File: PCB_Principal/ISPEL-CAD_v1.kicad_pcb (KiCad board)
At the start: 2 copper layers, 130 x 160 mm, 175 parts, among them J1 Vin, J10 CN7_NUCLEO, J11 CN10_NUCLEO, J12 GND_NUCLEO, J13 E1, J14 S1, J15 E2, J16 S2, J17 FRENTE, J18 PRUEBA_5V, J2 V5, J3 VREG, J4 TEMP, J5 GND_NUCLEO, J6 CN8_NUCLEO, J7 CN9_NUCLEO, J8 GND_NUCLEO, J9 GND_NUCLEO, Q201 BC807, Q202 BC559C, Q203 BC549C, Q204 BC549C, Q205 BC559C, Q206 2SD882, Q207 2SB772, Q251 BC807, Q252 BC559C, Q253 BC549C, Q254 BC549C, Q255 BC559C, Q256 2SD882, Q257 2SB772, U1 LM350_TO220, U101 TL071, U151 TL071, U2 LM350_TO220, U201 LM318, U251 LM318, U3 LM337_TO220, U301 TLV3501AID, U4 LM1117DT-5.0, U5 TL431DBZ

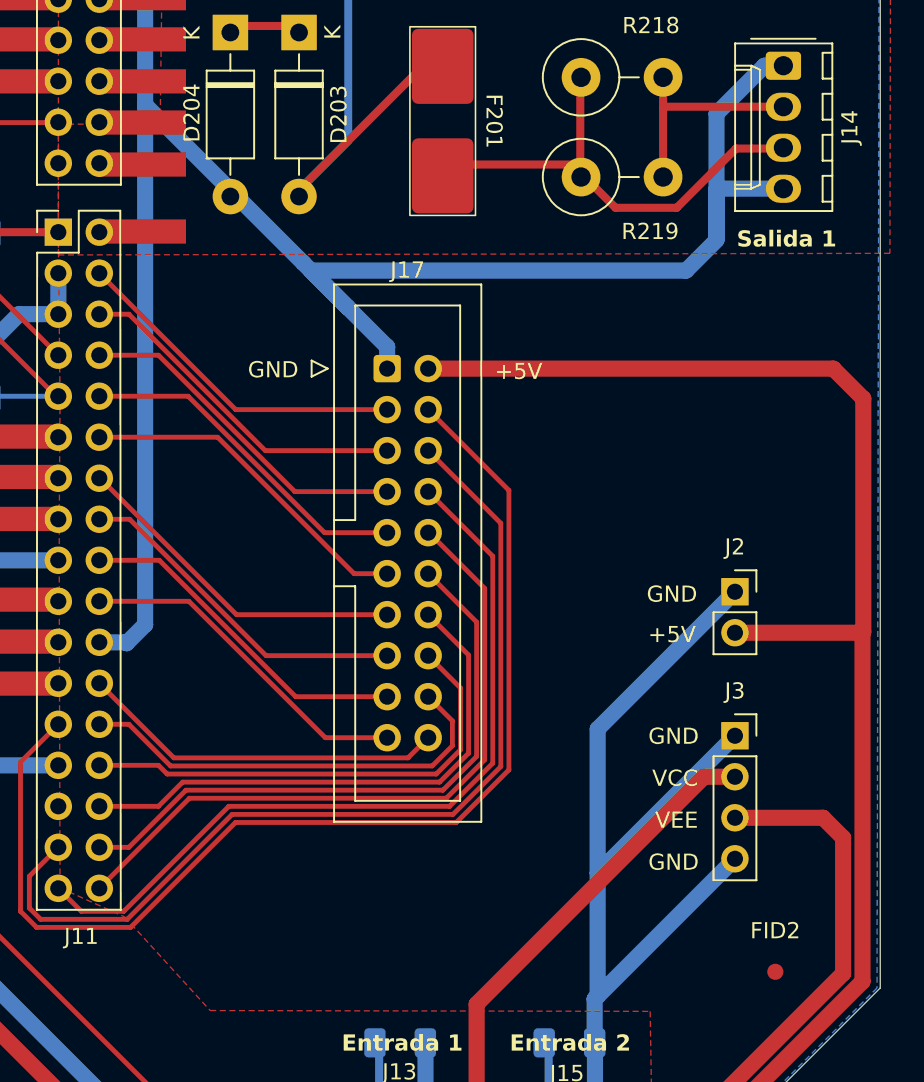
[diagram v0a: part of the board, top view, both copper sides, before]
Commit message: Corrigiendo PCB con comentarios AS.
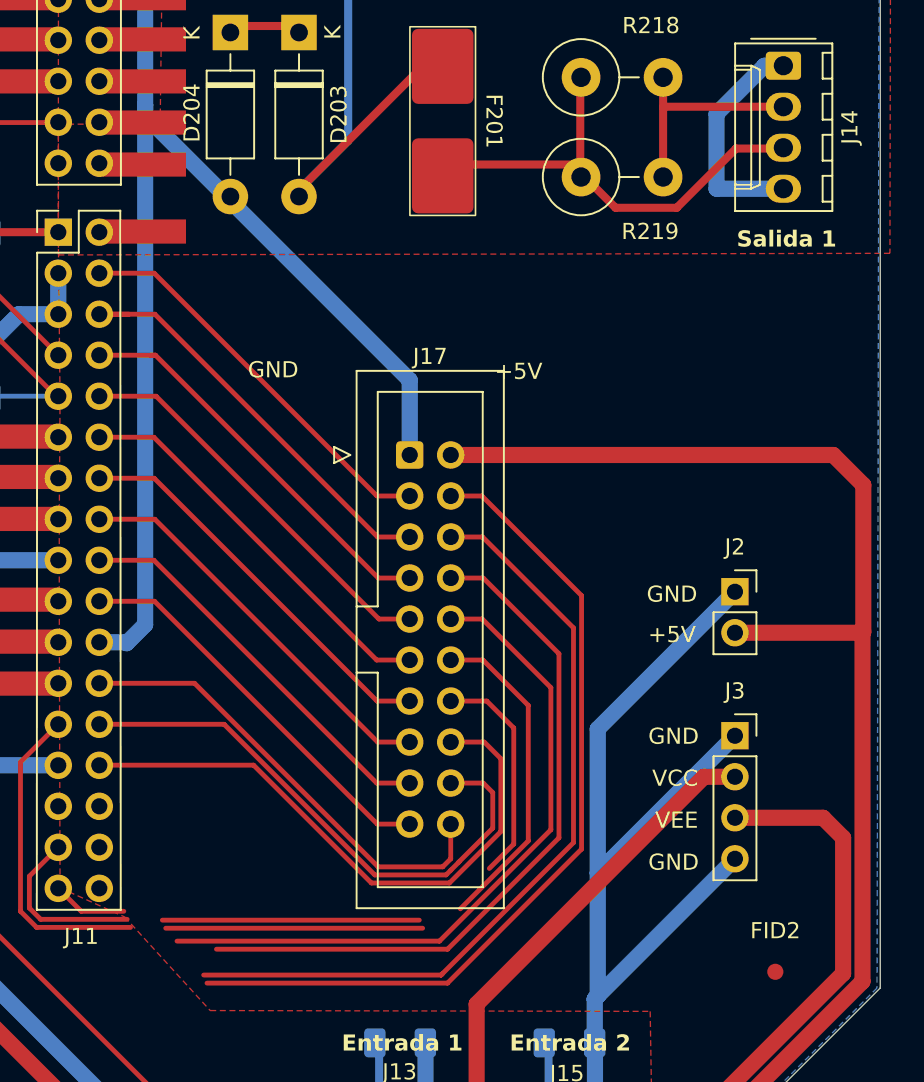
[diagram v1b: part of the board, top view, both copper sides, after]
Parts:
- moved J17 5.53 mm to (130.9, 127.0)
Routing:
- net GND: track 1466.8 -> 1437.3 mm
- net /LED7: track 30.4 -> 37.8 mm
- net /LED8: track 27.1 -> 34.5 mm
- net V5: track 521.0 -> 514.2 mm
- net /LED9: track 22.8 -> 28.8 mm
- net /BTN2: track 21.3 -> 25.9 mm
- net /LED6: track 33.8 -> 29.8 mm
- net /BTN3: track 21.3 -> 25.3 mm
- net /BTN6: track 21.3 -> 25.0 mm
- net /BTN5: track 21.3 -> 25.0 mm
- net /BTN7: track 21.3 -> 24.9 mm
- net /BTN4: track 21.3 -> 24.9 mm
- net /BTN9: track 21.3 -> 24.9 mm
- net /BTN8: track 21.3 -> 24.9 mm
- net /BTN1: track 21.3 -> 24.9 mm
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
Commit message: Corrigiendo anotaciones.
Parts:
- added H5: MountingHole, MountingHole:MountingHole_3.2mm_M3, F.Cu at (97.3, 131.7)
- added R14: 0, Resistor_SMD:R_1206_3216Metric_Pad1.30x1.75mm_HandSolder, F.Cu at (55.9, 113.2)
- R218, R219, R268, R269: footprint Resistor_THT:R_Axial_DIN0414_L11.9mm_D4.5mm_P5.08mm_Vertical -> Resistor_THT:R_Axial_DIN0414_L11.9mm_D4.5mm_P15.24mm_Horizontal
- moved R218 19.1 mm to (146.6, 122.0), turned to 90 degrees
- moved R268 13.0 mm to (146.7, 100.5), turned to 90 degrees
- moved R219 12.3 mm to (140.4, 122.0), turned to 90 degrees
- moved C257 9.73 mm to (126.8, 54.8), turned to 0 degrees
- moved C207 9.27 mm to (79.3, 54.0)
- moved J14 7.71 mm to (154.0, 110.6)
- moved R269 5.83 mm to (140.4, 100.5), turned to 90 degrees
- moved FID1 3.82 mm to (44.5, 37.9)
- moved R13 1.90 mm to (54.7, 99.9)
- moved R211 1.60 mm to (83.1, 54.0)
- moved R213 1.60 mm to (87.1, 54.0)
- moved R304 1.31 mm to (48.8, 162.3)
- moved R305 1.31 mm to (48.8, 159.1)
- moved J16 1.20 mm to (154.0, 89.1)
- moved F301 0.70 mm to (47.8, 171.8)
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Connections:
- J6 pad 15: V7 -> Net-(J6-Pin_15)
- R13 pad 1: V7 -> V5
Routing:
- net GND: track 1437.3 -> 1479.4 mm
- net VEE: track 638.6 -> 657.3 mm
- net S1_B: track 29.7 -> 45.9 mm
- net V7: track 91.9 -> 81.4 mm, vias 1 -> 0
- net /LED6: track 29.8 -> 40.1 mm
- net S2_B: track 29.5 -> 37.2 mm
- net /LED5: track 36.2 -> 42.7 mm
- net VCC: track 571.8 -> 578.0 mm
- net Net-(J6-Pin_15): track 0.00 -> 5.98 mm
- net Net-(Q203-B): track 28.6 -> 32.6 mm
- net S1_50: track 13.7 -> 17.5 mm
- net /LED3: track 48.8 -> 52.5 mm
- net V5: track 514.2 -> 510.7 mm
- net /LED4: track 42.8 -> 45.4 mm
- net S2_50: track 15.7 -> 18.0 mm
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- added copper zone on F.Cu, net V7
- added copper zone on F.Cu, net VCC
- added copper zone on F.Cu, net VEE
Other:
- board text added: "+7V"
- board text added: "ENTRADA 1"
- board text added: "ENTRADA 2"
- board text added: "FRENTE"
- board text added: "LADO INFERIOR"
- board text added: "LADO SUPERIOR"
- board text added: "LIMITE PLACA NUCLEO-144"
- board text added: "PRUEBA"
- board text added: "SALIDA 1"
- board text added: "SALIDA 2"
- board text removed: "Entrada 1"
- board text removed: "Entrada 2"
- board text removed: "Prueba"
- board text removed: "Salida 1"
- board text removed: "Salida 2"
- board text removed: "V7"

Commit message: Agregado de zócalo +7V y pruebas.
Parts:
- added J2: V7, Connector_PinSocket_2.54mm:PinSocket_1x02_P2.54mm_Vertical, F.Cu at (45.4, 95.1)
- moved C8 3.04 mm to (54.8, 65.1)
- moved R14 1.10 mm to (54.8, 113.1)
- moved J3 0.60 mm to (45.4, 99.9)
- renumbered J9 to J10, J10 to J11, J11 to J12, J12 to J13, J13 to J14, J14 to J15, J15 to J16, J16 to J17, J17 to J18, J18 to J19, J4 to J3, J3 to J4, J2 to J5, J5 to J6, J6 to J7, J7 to J8, J8 to J9
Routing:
- net V7: track 81.4 -> 88.8 mm
- net GND: track 1479.4 -> 1485.3 mm
- net Net-(J7-Pin_15): track 5.98 -> 7.10 mm
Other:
- board text added: "+3V3R"

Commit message: Versión 1 - ISPEL Beta 2024 para fabricar.
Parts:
- added R15: 1, Resistor_SMD:R_1206_3216Metric_Pad1.30x1.75mm_HandSolder, F.Cu at (151.3, 127.0)
- added RT1: 1, Resistor_SMD:R_1206_3216Metric_Pad1.30x1.75mm_HandSolder, F.Cu at (136.9, 46.4)
- added RT2: 1, Resistor_SMD:R_1206_3216Metric_Pad1.30x1.75mm_HandSolder, F.Cu at (153.8, 78.2)
- added RT3: 1, Resistor_SMD:R_1206_3216Metric_Pad1.30x1.75mm_HandSolder, F.Cu at (48.8, 154.8)
- added RT4: 1, Resistor_SMD:R_1206_3216Metric_Pad1.30x1.75mm_HandSolder, F.Cu at (86.5, 144.0)
- added RT5: 1, Resistor_SMD:R_1206_3216Metric_Pad1.30x1.75mm_HandSolder, F.Cu at (74.0, 137.7)
- moved H5 3.36 mm to (97.0, 135.0)
- moved FID2 2.45 mm to (151.1, 158.9)
- moved C101 1.95 mm to (130.3, 161.4)
- moved C151 1.95 mm to (140.8, 161.4)
- moved J14 1.95 mm to (131.5, 167.6)
- moved J16 1.95 mm to (142.0, 167.6)
- moved R301 1.01 mm to (56.8, 160.7)
- moved R303 1.01 mm to (61.5, 160.7)
- moved C102 0.50 mm to (88.6, 134.8)
- moved R102 0.50 mm to (88.7, 125.3)
- moved R101 0.50 mm to (88.7, 130.1)
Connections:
- J18 pad 2: V5 -> Net-(J18-Pin_2)
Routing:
- net V5: track 510.8 -> 494.3 mm
- net Net-(J18-Pin_2): track 0.00 -> 16.4 mm
- net VCC: track 578.1 -> 573.1 mm
- net GND: track 1485.3 -> 1489.6 mm
- net E2: track 62.0 -> 64.0 mm
- net Net-(R304-Pad1): track 24.7 -> 23.2 mm
- net E1: track 67.8 -> 66.9 mm
- net VEE: track 657.3 -> 658.0 mm
- net Net-(D101-A): track 17.9 -> 18.5 mm
- net Net-(U301-+): track 24.5 -> 25.0 mm
